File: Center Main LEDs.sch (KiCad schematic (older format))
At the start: 60 parts

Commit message: Schematic completed first draft
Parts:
- removed D?: LED F5, symbol Device:LED
- removed D?: LED 8, symbol Device:LED
- removed D?: LED 9, symbol Device:LED
- removed D?: LED Y, symbol Device:LED
- removed D?: LED J, symbol Device:LED
- removed D?: LED ,, symbol Device:LED
- removed R? (x3): 1.8k, symbol Device:R
- added D?: LED F5, symbol Device:LED
- added D?: LED 8, symbol Device:LED
- added D?: LED 9, symbol Device:LED
- added D?: LED Y, symbol Device:LED
- added D?: LED J, symbol Device:LED
- added D?: LED ,, symbol Device:LED
- added R? (x3): 1.8k, symbol Device:R
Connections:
- net DIMMER: now also R?.2, R?.2, R?.2
- net GND: now also D?.1 (K), D?.1 (K), D?.1 (K), D?.1 (K), D?.1 (K), D?.1 (K), D?.1 (K)
- net at D?.2 (A): now also R?.1 (x2)
- net at R?.1: now also D?.2 (A) (x5)
- new net: D?.2 (A), R?.1
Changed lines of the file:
@@
 $Descr B 17000 11000
 encoding utf-8
-Sheet 6 12
+Sheet 6 18
 Title ""
 Date ""
@@
 $Comp
 L Device:R R?
-U 1 1 5EA03178
+U 1 1 60A6F954
 P 7500 2000
-AR Path="/5E8C7194/60C027BD/5EA03178" Ref="R?"  Part="1"
-AR Path="/5E8C755A/5E9909EC/5EA03178" Ref="R?"  Part="1"
+AR Path="/5E8C7194/60C027BD/60A6F954" Ref="R?"  Part="1"
+AR Path="/5E8C755A/5E9909EC/60A6F954" Ref="R?"  Part="1"
 F 0 "R?" V 7293 2000 50  0000 C CNN
 F 1 "1.8k" V 7384 2000 50  0000 C CNN
@@
 $Comp
 L Device:LED D?
-U 1 1 5EA0317E
+U 1 1 60A6F955
 P 8000 2000
-AR Path="/5E8C7194/60C027BD/5EA0317E" Ref="D?"  Part="1"
-AR Path="/5E8C755A/5E9909EC/5EA0317E" Ref="D?"  Part="1"
+AR Path="/5E8C7194/60C027BD/60A6F955" Ref="D?"  Part="1"
+AR Path="/5E8C755A/5E9909EC/60A6F955" Ref="D?"  Part="1"
 F 0 "D?" H 7993 1745 50  0000 C CNN
 F 1 "LED F5" H 7993 1836 50  0000 C CNN
@@
 $Comp
 L Device:R R?
-U 1 1 5EA1C32B
+U 1 1 60A6F95C
 P 7500 3000
-AR Path="/5E8C7194/60C027BD/5EA1C32B" Ref="R?"  Part="1"
-AR Path="/5E8C755A/5E9909EC/5EA1C32B" Ref="R?"  Part="1"
+AR Path="/5E8C7194/60C027BD/60A6F95C" Ref="R?"  Part="1"
+AR Path="/5E8C755A/5E9909EC/60A6F95C" Ref="R?"  Part="1"
 F 0 "R?" V 7293 3000 50  0000 C CNN
 F 1 "1.8k" V 7384 3000 50  0000 C CNN
@@
 $Comp
 L Device:LED D?
-U 1 1 5EA1C353
+U 1 1 60A6F961
 P 11000 3000
-AR Path="/5E8C7194/60C027BD/5EA1C353" Ref="D?"  Part="1"
-AR Path="/5E8C755A/5E9909EC/5EA1C353" Ref="D?"  Part="1"
+AR Path="/5E8C7194/60C027BD/60A6F961" Ref="D?"  Part="1"
+AR Path="/5E8C755A/5E9909EC/60A6F961" Ref="D?"  Part="1"
 F 0 "D?" H 10993 2745 50  0000 C CNN
 F 1 "LED 8" H 10993 2836 50  0000 C CNN
@@
 $Comp
 L Device:LED D?
-U 1 1 5EA1C364
+U 1 1 60A6F963
 P 12500 3000
-AR Path="/5E8C7194/60C027BD/5EA1C364" Ref="D?"  Part="1"
-AR Path="/5E8C755A/5E9909EC/5EA1C364" Ref="D?"  Part="1"
+AR Path="/5E8C7194/60C027BD/60A6F963" Ref="D?"  Part="1"
+AR Path="/5E8C755A/5E9909EC/60A6F963" Ref="D?"  Part="1"
 F 0 "D?" H 12493 2745 50  0000 C CNN
 F 1 "LED 9" H 12493 2836 50  0000 C CNN
@@
 $Comp
 L Device:LED D?
-U 1 1 5EA542F1
+U 1 1 60A6F965
 P 9500 4000
-AR Path="/5E8C7194/60C027BD/5EA542F1" Ref="D?"  Part="1"
-AR Path="/5E8C755A/5E9909EC/5EA542F1" Ref="D?"  Part="1"
+AR Path="/5E8C7194/60C027BD/60A6F965" Ref="D?"  Part="1"
+AR Path="/5E8C755A/5E9909EC/60A6F965" Ref="D?"  Part="1"
 F 0 "D?" H 9493 3745 50  0000 C CNN
 F 1 "LED Y" H 9493 3836 50  0000 C CNN
@@
 $Comp
 L Device:R R?
-U 1 1 5EA58CE7
+U 1 1 60A6F96A
 P 9000 5000
-AR Path="/5E8C7194/60C027BD/5EA58CE7" Ref="R?"  Part="1"
-AR Path="/5E8C755A/5E9909EC/5EA58CE7" Ref="R?"  Part="1"
+AR Path="/5E8C7194/60C027BD/60A6F96A" Ref="R?"  Part="1"
+AR Path="/5E8C755A/5E9909EC/60A6F96A" Ref="R?"  Part="1"
 F 0 "R?" V 8793 5000 50  0000 C CNN
 F 1 "1.8k" V 8884 5000 50  0000 C CNN
@@
 $Comp
 L Device:LED D?
-U 1 1 5EA58CFE
+U 1 1 60A6F96D
 P 11000 5000
-AR Path="/5E8C7194/60C027BD/5EA58CFE" Ref="D?"  Part="1"
-AR Path="/5E8C755A/5E9909EC/5EA58CFE" Ref="D?"  Part="1"
+AR Path="/5E8C7194/60C027BD/60A6F96D" Ref="D?"  Part="1"
+AR Path="/5E8C755A/5E9909EC/60A6F96D" Ref="D?"  Part="1"
 F 0 "D?" H 10993 4745 50  0000 C CNN
 F 1 "LED J" H 10993 4836 50  0000 C CNN
@@
 Wire Wire Line
 	4200 6000 4200 5650
-Wire Wire Line
-	9050 6000 9050 6350
 $Comp
 L Device:R R?
@@
 $Comp
 L Device:LED D?
-U 1 1 5EA5F3B3
+U 1 1 60A6F975
 P 12500 6000
-AR Path="/5E8C7194/60C027BD/5EA5F3B3" Ref="D?"  Part="1"
-AR Path="/5E8C755A/5E9909EC/5EA5F3B3" Ref="D?"  Part="1"
+AR Path="/5E8C7194/60C027BD/60A6F975" Ref="D?"  Part="1"
+AR Path="/5E8C755A/5E9909EC/60A6F975" Ref="D?"  Part="1"
 F 0 "D?" H 12493 5745 50  0000 C CNN
 F 1 "LED ," H 12493 5836 50  0000 C CNN
@@
 Connection ~ 6800 6350
 Wire Wire Line
-	6800 6350 3850 6350
+	6800 6350 5300 6350
 Connection ~ 8300 6350
 Wire Wire Line
 	8300 6350 6800 6350
-Connection ~ 9050 6350
-Wire Wire Line
-	9050 6350 8300 6350
 Connection ~ 9800 6350
-Wire Wire Line
-	9800 6350 9050 6350
 Connection ~ 11300 6350
 Wire Wire Line
@@
 Wire Wire Line
 	10200 2650 8700 2650
+Wire Wire Line
+	5300 6000 5300 6350
+Connection ~ 5300 6350
+Wire Wire Line
+	5300 6350 3850 6350
+Wire Wire Line
+	8300 6350 9800 6350
 $EndSCHEMATC

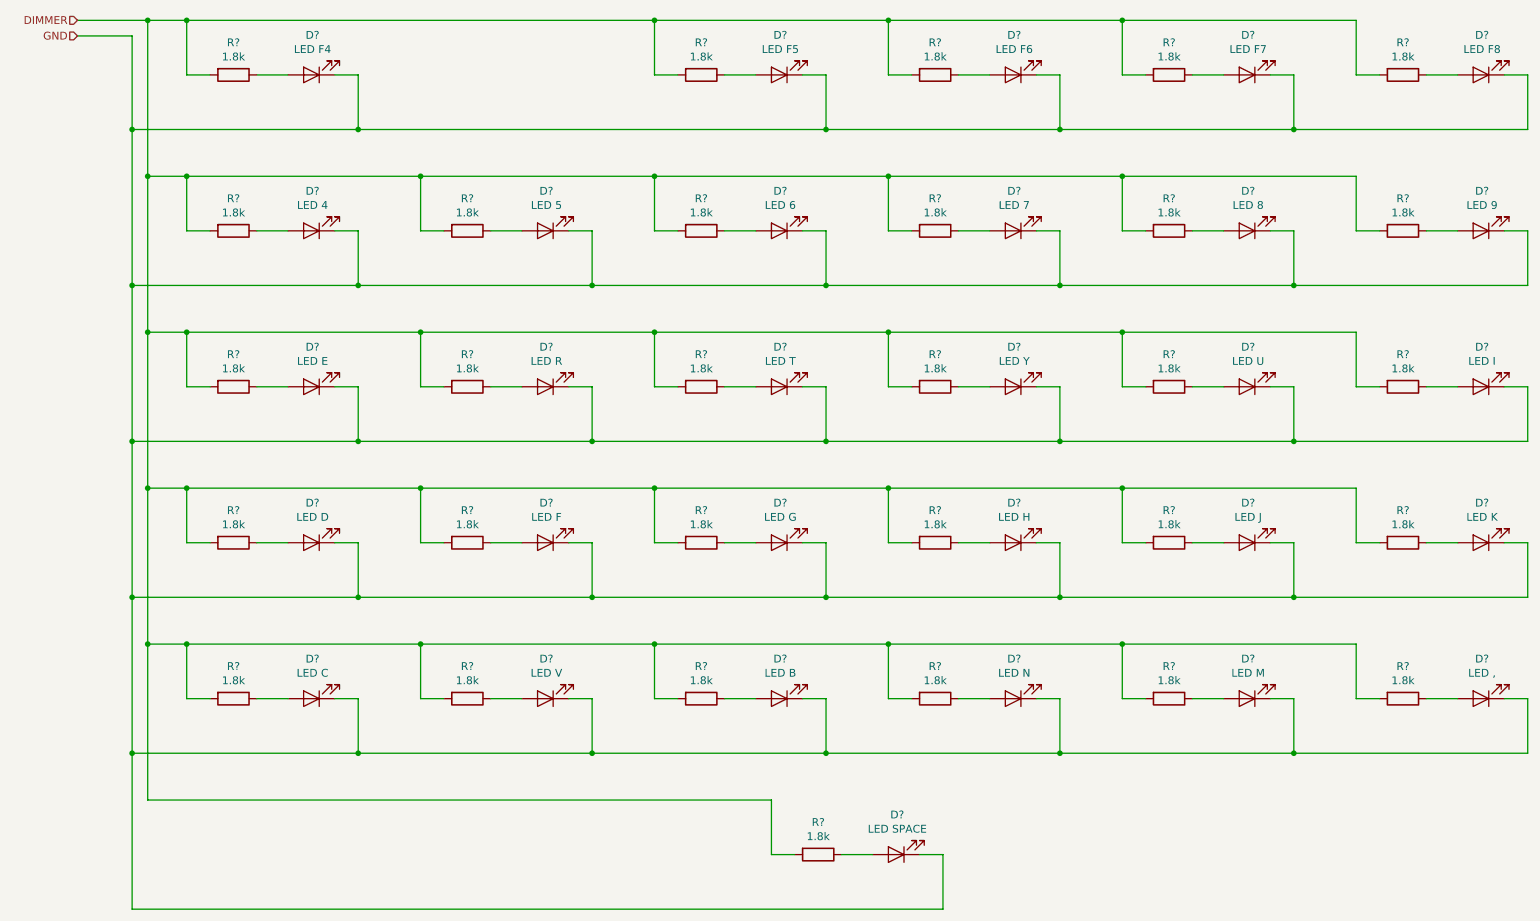
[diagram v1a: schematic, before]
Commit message: Corrected errors found in design rule check
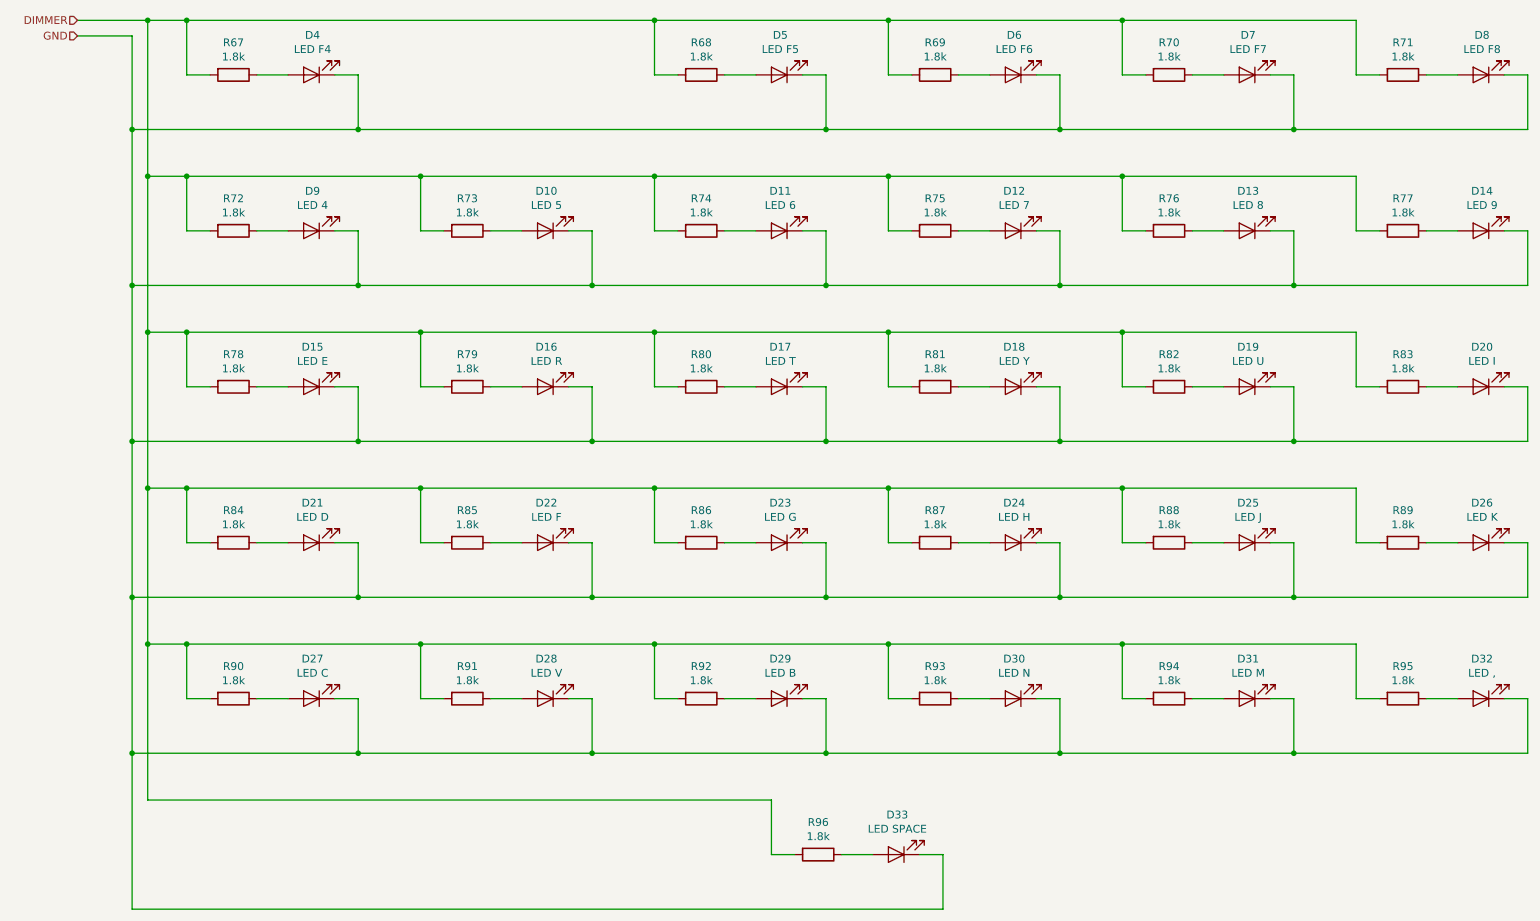
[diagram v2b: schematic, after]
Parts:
- D10, D11, D12, D13, D14, D15, D16, D17, D18, D19, D20, D21, D22, D23, D24, D25, D26, D27, D28, D29, D30, D31, D32, D33, D4, D5, D6, D7, D8, D9: renamed from D?; footprint (none) -> LED_SMD:LED_1206_3216Metric_ReverseMount_Hole1.8x2.4mm
- R67, R68, R69, R70, R71, R72, R73, R74, R75, R76, R77, R78, R79, R80, R81, R82, R83, R84, R85, R86, R87, R88, R89, R90, R91, R92, R93, R94, R95, R96: renamed from R?; footprint (none) -> Resistor_SMD:R_1206_3216Metric_Pad1.42x1.75mm_HandSolder
